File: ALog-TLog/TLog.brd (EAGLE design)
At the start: 124.1 x 45.3 mm, 106 parts, among them IC1 ATMEGA644M, J6 5.5x2.1mm Barrel, Q1 220mA/50V/3.5Ω, Q5 MOSFET_PCH-IRLML2244, Q6 MOSFET_PCH-IRLML2244, Q7 MOSFET_PCH-IRLML2244, Q8 MOSFET-NCH-BSS138, Q9 MOSFET-NCH-BSS138, U2 FT231X-Q, U3 915MHz, U4 SX1509, X2 87832-14

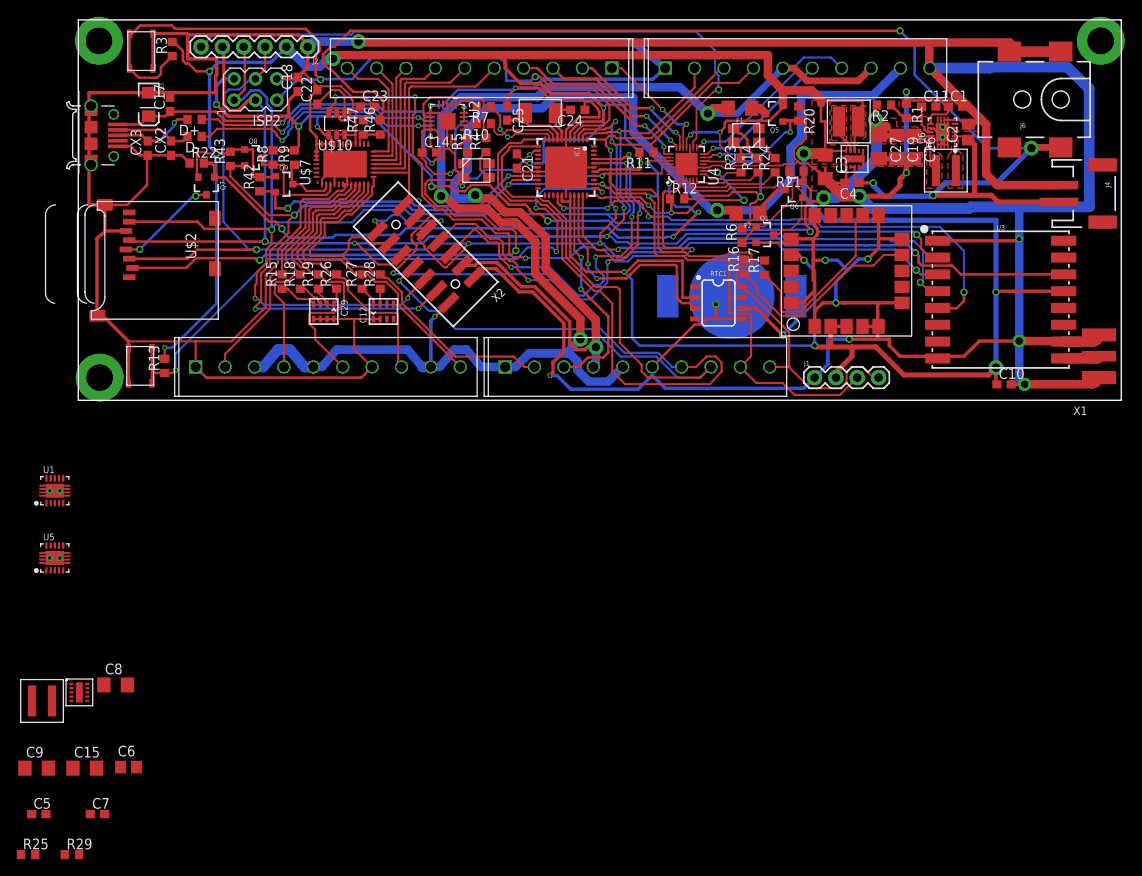
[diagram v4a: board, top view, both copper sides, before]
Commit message: updated 3.3V regulator
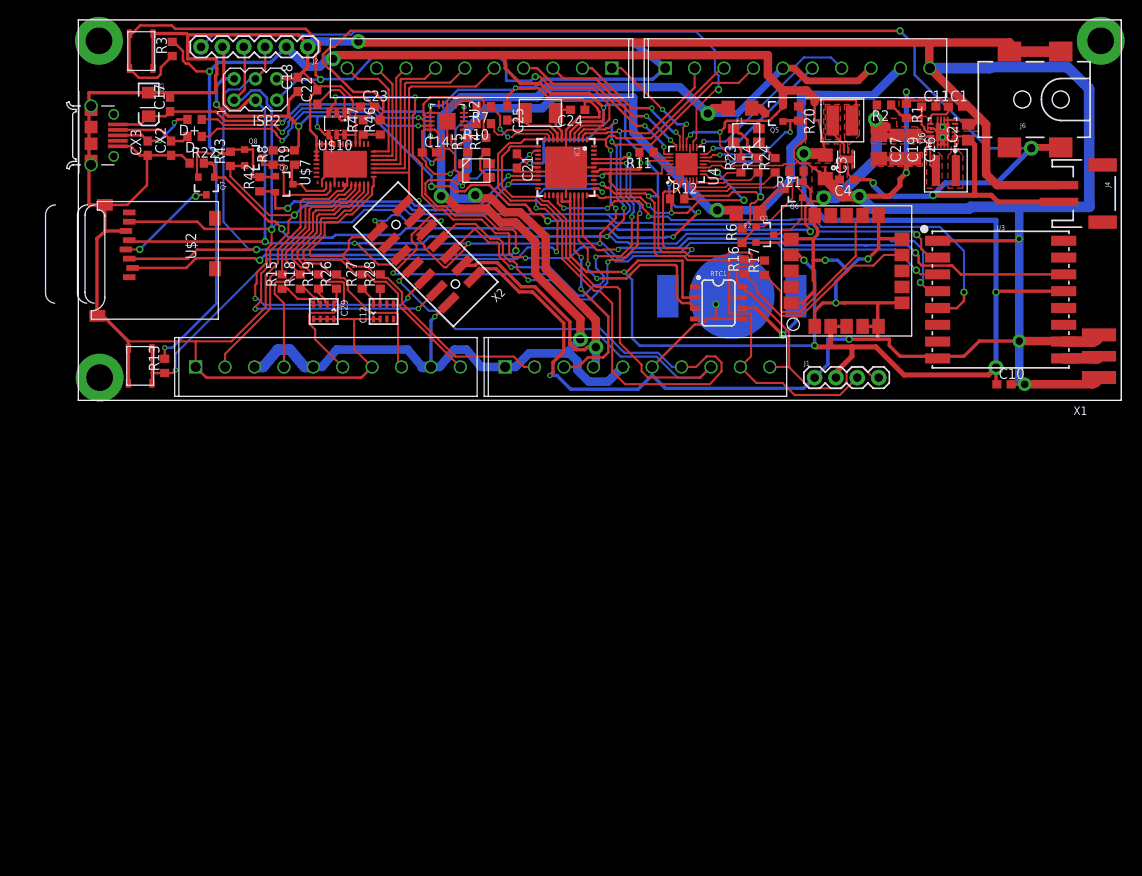
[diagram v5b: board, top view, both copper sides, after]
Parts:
- removed C15, C8, C9: 22uF, rcl:C1206
- removed C5: 0.1uF, rcl:C0603
- removed C6: 10uF, rcl:C0805
- removed C7: 10pF, rcl:C0603
- removed R25: 143k, rcl:R0603
- removed R29: 953k, rcl:R0603
- removed U$13: TPS63061, bschulz:WSON-10
- removed U$17: 1uH, bschulz:WE-MAIA(4.1X4.1)
- removed U1, U5: (no value), microbuilder:PWSON-N10
- U$4: value TPS6217XTPS62177 -> TPS62172; device bschulz:WSON-10 -> SparkFun-IC-Power:WSON-8-PAD
- moved U$4 1.02 mm to (91.5, 28.8), turned to 0 degrees
- moved L2 0.77 mm to (91.1, 33.4)
- moved C4 0.74 mm to (91.6, 26.4)
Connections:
- removed net N$29: U5.10
- removed net N$33: U$13.P$10, U$17.P$2
- removed net N$34: U$13.P$1, U$17.P$1
- removed net N$40: C5.1, U$13.P$6
- removed net N$42: C7.1, R25.2, R29.1, U$13.P$8
- removed net PGND: U1.THERMAL@1, U1.THERMAL@10, U1.THERMAL@11, U1.THERMAL@12, U1.THERMAL@13, U1.THERMAL@14, U1.THERMAL@5, U1.THERMAL@6, U1.THERMAL@7, U1.THERMAL@8, U1.THERMAL@9, U5.THERMAL@1, U5.THERMAL@10, U5.THERMAL@11, U5.THERMAL@12, U5.THERMAL@13, U5.THERMAL@14, U5.THERMAL@5, U5.THERMAL@6, U5.THERMAL@7, U5.THERMAL@8, U5.THERMAL@9
- removed net VIN: U1.2, U5.2
- removed net VOUT: U1.9, U5.9
- net 3V3: now also U$4.6; no longer U$4.P$10, U$4.P$8
- net 5V: no longer C15.1, C8.1, C9.1, R29.2, U$13.P$9
- net BATT+: now also U$4.2, U$4.3; no longer C6.1, U$13.P$2, U$13.P$3, U$4.P$2, U$4.P$3
- net GND: now also U$4.1, U$4.4, U$4.5, U$4.PAD; no longer C15.2, C5.2, C6.2, C7.2, C8.2, C9.2, R25.1, U$13.P$11, U$13.P$4, U$13.P$7, U$4.P$1, U$4.P$11, U$4.P$4, U$4.P$5, U$4.P$6, U1.7, U5.7
- net N$2: now also U$4.7; no longer U$4.P$9
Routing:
- net 3V3: track 434.7 -> 430.3 mm
- net GND: track 842.5 -> 840.5 mm
- net BATT+: track 160.9 -> 161.4 mm

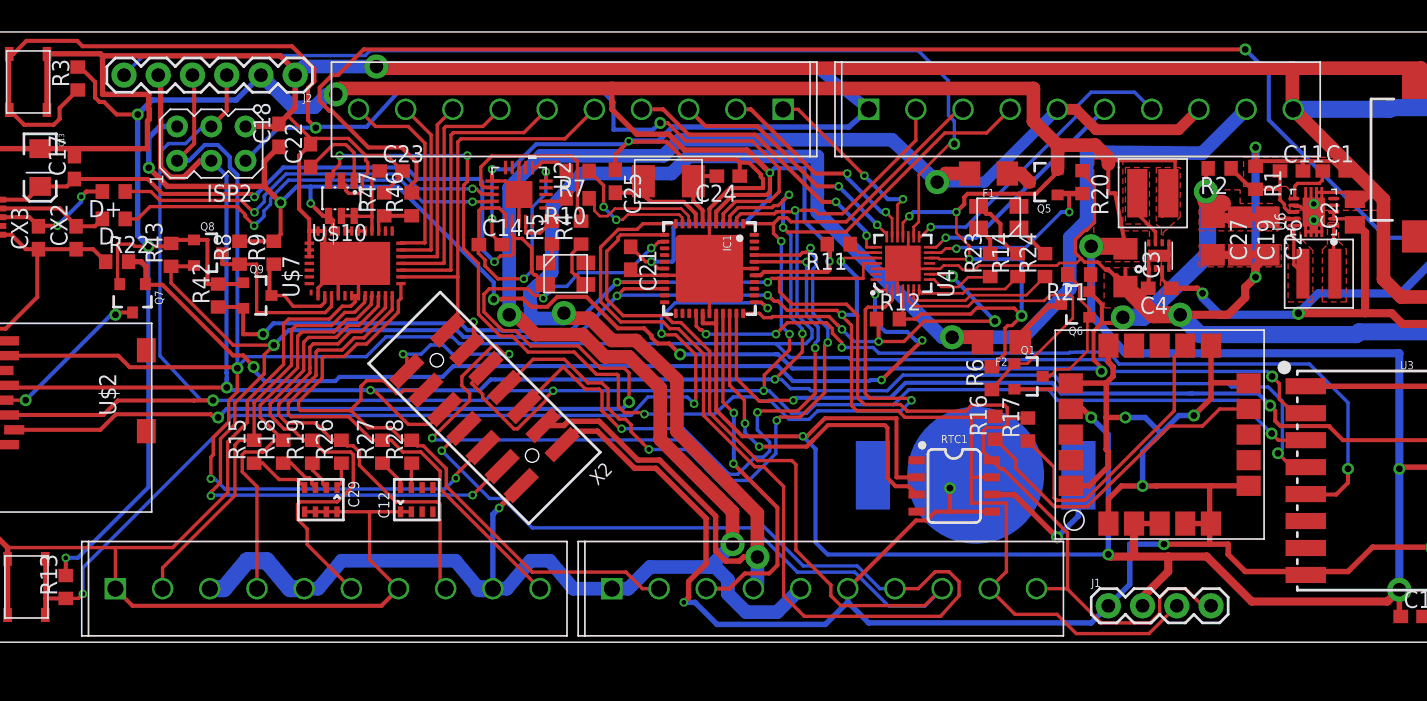
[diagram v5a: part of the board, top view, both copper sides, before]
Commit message: Fixed silkscreen, ready for prototype
Flipped/moved some of the silkscreen and checked DRC, ready to send for prototype
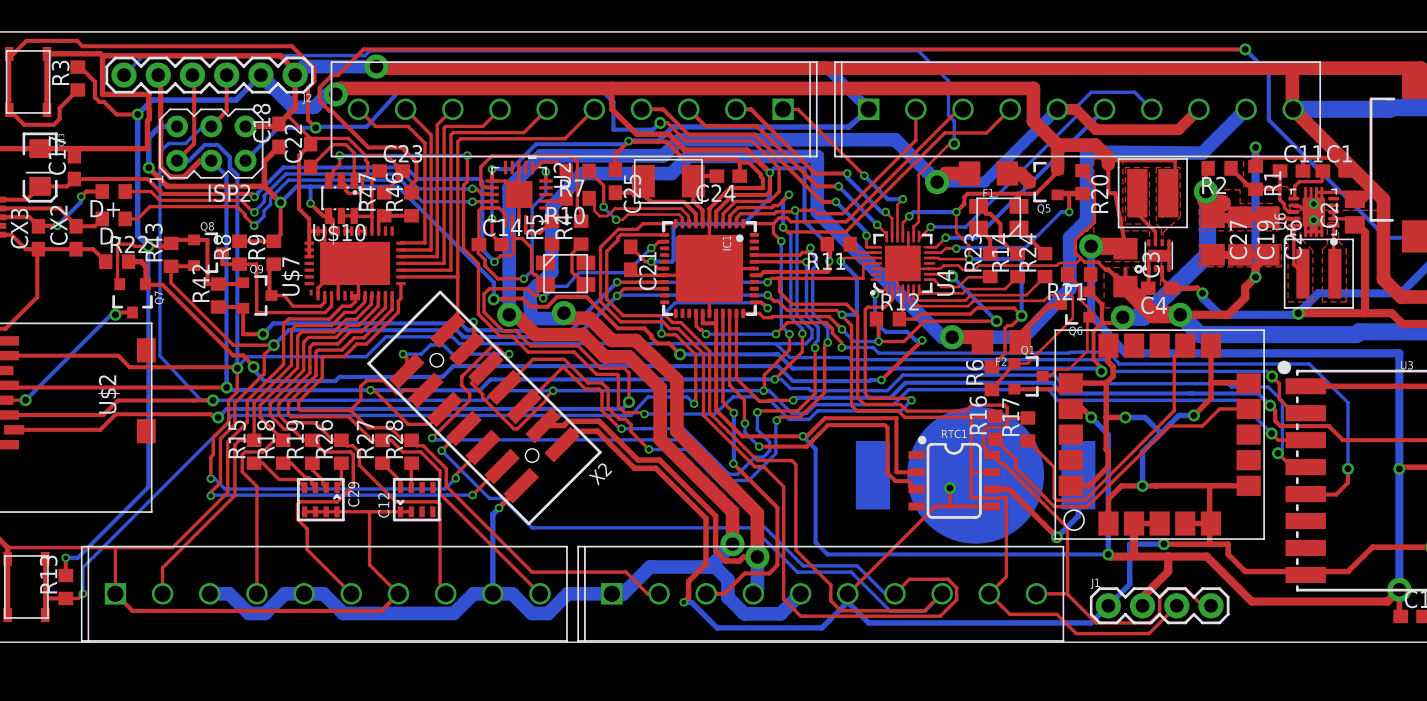
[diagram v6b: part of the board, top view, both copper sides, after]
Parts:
- moved J8 0.38 mm to (14.1, 3.68)
- moved J9 0.38 mm to (50.9, 3.68)
- moved RTC1 0.38 mm to (76.3, 12.1)
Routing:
- net EXT_3.3V: track 160.6 -> 159.2 mm
- net GND: track 840.5 -> 841.2 mm
- net TX_EXT: track 94.9 -> 95.4 mm
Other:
- board text added: "D4"
- board text added: "D5"
- board text removed: "CS2"
- board text removed: "D6"

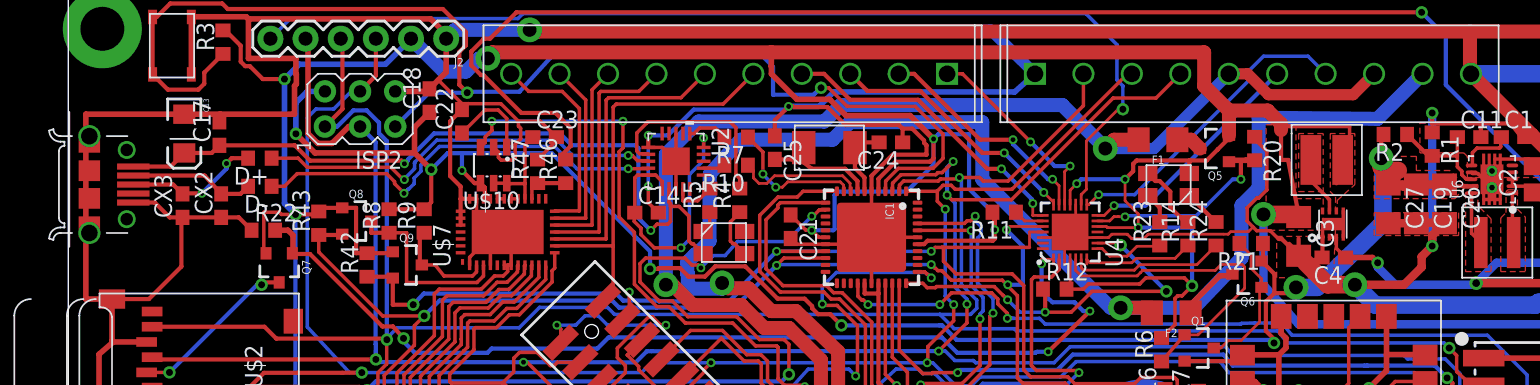
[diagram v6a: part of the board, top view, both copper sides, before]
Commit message: Added documentation so BOM auto-generates
Added attributes to parts to that when the BOM ULP is run, Digikey PNs are auto added along with other info.
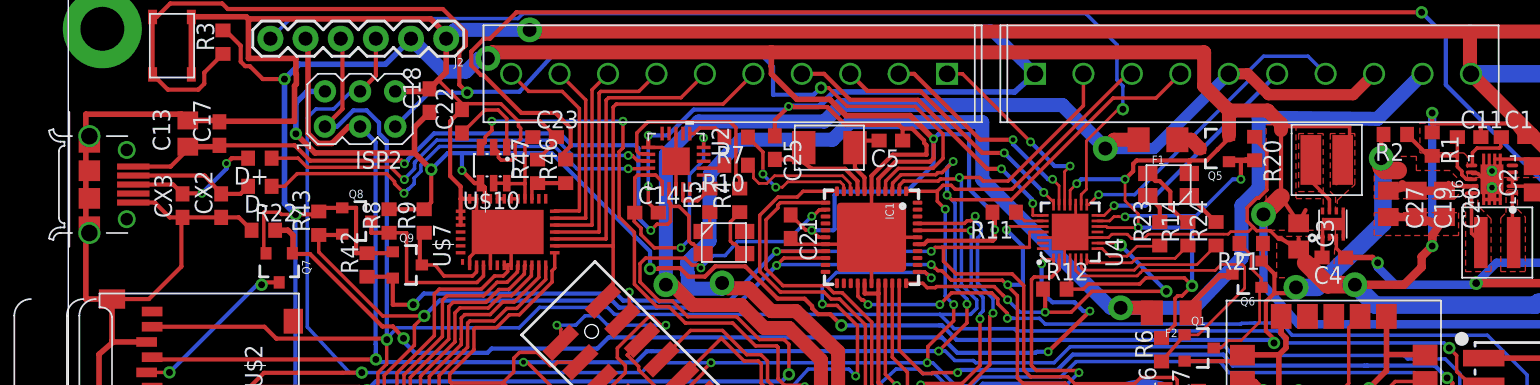
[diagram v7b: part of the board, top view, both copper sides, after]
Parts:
- removed C24: (no value), rcl:C0603
- added C5: 12pF, rcl:C0603
- BT1: value LINX-BAT-HLD-012-SMT-OTL -> BATTERY_COIN12MM; device awickert:LINX_BAT-HLD-012-SMT -> bschulz:AWICKERT_LINX_BAT-HLD-012-SMT
- C1, C10, C11, C18, C21, C22, C23, C4: device rcl:C0603 -> bschulz:C0603
- C13: device SparkFun-Passives:EIA3216 -> bschulz:C0805
- C14, C17: device resistor:C0603 -> bschulz:C0603
- C19, C26, C27, C3: device rcl:C1206 -> bschulz:C0805
- C2: device rcl:C0805 -> bschulz:C0805
- C25: value (none) -> 12pF
- CX2, CX3: value 33pF -> 12pF; device resistor:C0603 -> bschulz:C0603
- D+, D-, R1, R11, R12, R15, R18, R19, R2, R20, R21, R22, R26, R27, R28, R3, R42, R43, R46, R47, R8, R9: device rcl:R0603 -> bschulz:R0603
- F1, F2: value 6V/0.5A -> PPTC_HALF-AMP; device SparkFun-Fuses:1206 -> bschulz:1206
- J4: device SparkFun-Connectors:JST-2-SMD -> bschulz:JST-2-SMD
- J6: device SparkFun-Connectors:POWER_JACK_SMD -> bschulz:POWER_JACK_SMD
- Q1: value 220mA/50V/3.5Ω -> MOSFET-NCH-BSS138; device SparkFun-DiscreteSemi:SOT23-3 -> bschulz:SOT23-3
- R10, R4, R5, R7: value 1k -> 330; device rcl:R0603 -> bschulz:R0603
- R13, R14, R23, R24, R6: device resistor:R0603 -> bschulz:R0603
- U$1: value CRYSTAL_5X3.2_2LEAD -> CRYSTALTXC_8MHZ
- U$4: value TPS62172 -> TPS62172-Q1; device SparkFun-IC-Power:WSON-8-PAD -> bschulz:WSON-8-PAD
- U$5, U$9: value SKRPABE010 -> SWITCHC&K_400GF; device bschulz:SKRPABE010_(SWITCH) -> bschulz:SWITCH_4.2X3.2
- U2: device FT231X:QFN20 -> bschulz:QFN20
- U6: device microbuilder:PWSON-N10 -> bschulz:MICROBUILDER_PWSON-N10
- X1: device adafruit:SMA_EDGELAUNCH -> bschulz:ADAFRUIT_SMA_EDGELAUNCH
- moved C13 0.25 mm to (8.76, 35.3), turned to 90 degrees
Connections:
- net GND: now also C13.2, C5.1; no longer C13.C, C24.1
- net N$5: now also C5.2; no longer C24.2
- net VUSB: now also C13.1; no longer C13.A
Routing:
- net GND: track 841.2 -> 841.8 mm
